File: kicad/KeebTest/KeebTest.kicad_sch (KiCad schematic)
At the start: 19 parts, among them U1 Arduino_Pro_Micro

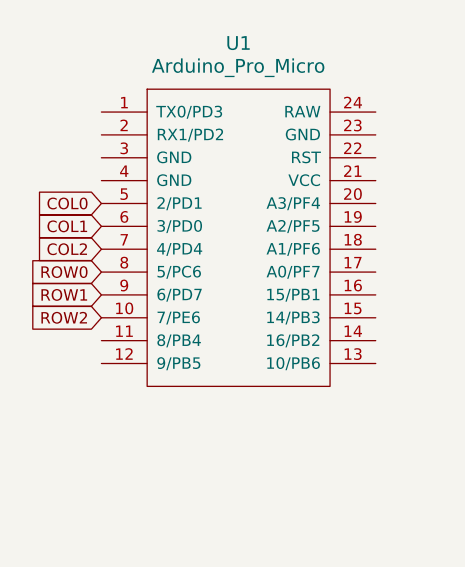
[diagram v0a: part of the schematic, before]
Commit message: update size
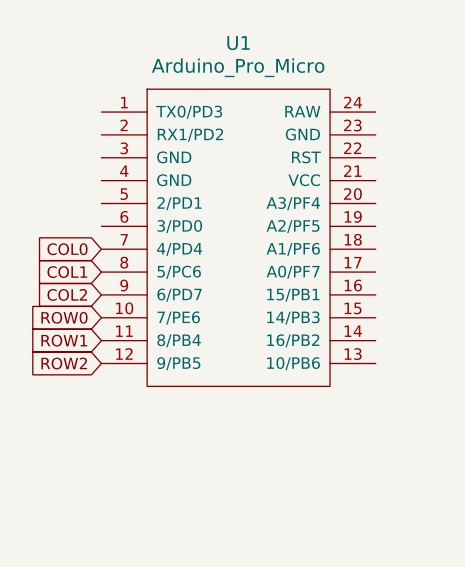
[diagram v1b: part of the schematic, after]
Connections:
- net COL0: now also U1.7 (4/PD4); no longer U1.5 (2/PD1)
- net COL1: now also U1.8 (5/PC6); no longer U1.6 (3/PD0)
- net COL2: now also U1.9 (6/PD7); no longer U1.7 (4/PD4)
- net ROW0: now also U1.10 (7/PE6); no longer U1.8 (5/PC6)
- net ROW1: now also U1.11 (8/PB4); no longer U1.9 (6/PD7)
- net ROW2: now also U1.12 (9/PB5); no longer U1.10 (7/PE6)
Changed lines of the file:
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@@
     (stroke (width 0) (type default))
   )
-  (global_label "COL0" (shape input) (at 30.48 57.15 180) (fields_autoplaced)
+  (global_label "ROW0" (shape input) (at 30.48 69.85 180) (fields_autoplaced)
     (effects (font (size 1.27 1.27)) (justify right))
-    (property "Intersheetrefs" "${INTERSHEET_REFS}" (at 22.6567 57.15 0)
+    (property "Intersheetrefs" "${INTERSHEET_REFS}" (at 22.2334 69.85 0)
       (effects (font (size 1.27 1.27)) (justify right) hide)
     )
   )
-  (global_label "COL1" (shape input) (at 30.48 59.69 180) (fields_autoplaced)
+  (global_label "ROW1" (shape input) (at 30.48 72.39 180) (fields_autoplaced)
     (effects (font (size 1.27 1.27)) (justify right))
-    (property "Intersheetrefs" "${INTERSHEET_REFS}" (at 22.6567 59.69 0)
+    (property "Intersheetrefs" "${INTERSHEET_REFS}" (at 22.2334 72.39 0)
       (effects (font (size 1.27 1.27)) (justify right) hide)
     )
   )
-  (global_label "ROW1" (shape input) (at 30.48 67.31 180) (fields_autoplaced)
+  (global_label "COL1" (shape input) (at 30.48 64.77 180) (fields_autoplaced)
     (effects (font (size 1.27 1.27)) (justify right))
-    (property "Intersheetrefs" "${INTERSHEET_REFS}" (at 22.2334 67.31 0)
+    (property "Intersheetrefs" "${INTERSHEET_REFS}" (at 22.6567 64.77 0)
+      (effects (font (size 1.27 1.27)) (justify right) hide)
+    )
+  )
+  (global_label "COL0" (shape input) (at 30.48 62.23 180) (fields_autoplaced)
+    (effects (font (size 1.27 1.27)) (justify right))
+    (property "Intersheetrefs" "${INTERSHEET_REFS}" (at 22.6567 62.23 0)
+      (effects (font (size 1.27 1.27)) (justify right) hide)
+    )
+  )
+  (global_label "ROW2" (shape input) (at 30.48 74.93 180) (fields_autoplaced)
+    (effects (font (size 1.27 1.27)) (justify right))
+    (property "Intersheetrefs" "${INTERSHEET_REFS}" (at 22.2334 74.93 0)
       (effects (font (size 1.27 1.27)) (justify right) hide)
     )
@@
     )
   )
-  (global_label "ROW2" (shape input) (at 30.48 69.85 180) (fields_autoplaced)
-    (effects (font (size 1.27 1.27)) (justify right))
-    (property "Intersheetrefs" "${INTERSHEET_REFS}" (at 22.2334 69.85 0)
-      (effects (font (size 1.27 1.27)) (justify right) hide)
-    )
-  )
   (global_label "ROW1" (shape input) (at 133.35 85.09 0) (fields_autoplaced)
     (effects (font (size 1.27 1.27)) (justify left))
     (property "Intersheetrefs" "${INTERSHEET_REFS}" (at 141.5966 85.09 0)
       (effects (font (size 1.27 1.27)) (justify left) hide)
-    )
-  )
-  (global_label "ROW0" (shape input) (at 30.48 64.77 180) (fields_autoplaced)
-    (effects (font (size 1.27 1.27)) (justify right))
-    (property "Intersheetrefs" "${INTERSHEET_REFS}" (at 22.2334 64.77 0)
-      (effects (font (size 1.27 1.27)) (justify right) hide)
     )
   )
@@
     )
   )
-  (global_label "COL2" (shape input) (at 30.48 62.23 180) (fields_autoplaced)
-    (effects (font (size 1.27 1.27)) (justify right))
-    (property "Intersheetrefs" "${INTERSHEET_REFS}" (at 22.6567 62.23 0)
-      (effects (font (size 1.27 1.27)) (justify right) hide)
-    )
-  )
   (global_label "ROW2" (shape input) (at 133.35 106.68 0) (fields_autoplaced)
     (effects (font (size 1.27 1.27)) (justify left))
@@
     )
   )
+  (global_label "COL2" (shape input) (at 30.48 67.31 180) (fields_autoplaced)
+    (effects (font (size 1.27 1.27)) (justify right))
+    (property "Intersheetrefs" "${INTERSHEET_REFS}" (at 22.6567 67.31 0)
+      (effects (font (size 1.27 1.27)) (justify right) hide)
+    )
+  )

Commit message: update size
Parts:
- added H1, H2, H3, H4: MountingHole, MountingHole:MountingHole_2.1mm, symbol Mechanical:MountingHole
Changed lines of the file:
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@@
+    )
+  )
+  (symbol (lib_id "Mechanical:MountingHole") (at 154.94 106.68 0) (unit 1)
+    (in_bom yes) (on_board yes) (dnp no) (fields_autoplaced)
+    (property "Reference" "H2" (at 157.48 105.41 0)
+      (effects (font (size 1.27 1.27)) (justify left))
+    )
+    (property "Value" "MountingHole" (at 157.48 107.95 0)
+      (effects (font (size 1.27 1.27)) (justify left))
+    )
+    (property "Footprint" "MountingHole:MountingHole_2.1mm" (at 154.94 106.68 0)
+      (effects (font (size 1.27 1.27)) hide)
+    )
+    (property "Datasheet" "~" (at 154.94 106.68 0)
+      (effects (font (size 1.27 1.27)) hide)
+    )
+    (instances
+      (project "KeebTest"
+        (path "/98130f4e-5d52-447d-b126-df1d975aefd0"
+          (reference "H2") (unit 1)
+        )
+      )
+    )
+  )
+  (symbol (lib_id "Mechanical:MountingHole") (at 152.4 30.48 0) (unit 1)
+    (in_bom yes) (on_board yes) (dnp no) (fields_autoplaced)
+    (property "Reference" "H1" (at 154.94 29.21 0)
+      (effects (font (size 1.27 1.27)) (justify left))
+    )
+    (property "Value" "MountingHole" (at 154.94 31.75 0)
+      (effects (font (size 1.27 1.27)) (justify left))
+    )
+    (property "Footprint" "MountingHole:MountingHole_2.1mm" (at 152.4 30.48 0)
+      (effects (font (size 1.27 1.27)) hide)
+    )
+    (property "Datasheet" "~" (at 152.4 30.48 0)
+      (effects (font (size 1.27 1.27)) hide)
+    )
+    (instances
+      (project "KeebTest"
+        (path "/98130f4e-5d52-447d-b126-df1d975aefd0"
+          (reference "H1") (unit 1)
+        )
+      )
     )
   )
@@
     )
   )
+  (symbol (lib_id "Mechanical:MountingHole") (at 27.94 106.68 0) (unit 1)
+    (in_bom yes) (on_board yes) (dnp no) (fields_autoplaced)
+    (property "Reference" "H3" (at 30.48 105.41 0)
+      (effects (font (size 1.27 1.27)) (justify left))
+    )
+    (property "Value" "MountingHole" (at 30.48 107.95 0)
+      (effects (font (size 1.27 1.27)) (justify left))
+    )
+    (property "Footprint" "MountingHole:MountingHole_2.1mm" (at 27.94 106.68 0)
+      (effects (font (size 1.27 1.27)) hide)
+    )
+    (property "Datasheet" "~" (at 27.94 106.68 0)
+      (effects (font (size 1.27 1.27)) hide)
+    )
+    (instances
+      (project "KeebTest"
+        (path "/98130f4e-5d52-447d-b126-df1d975aefd0"
+          (reference "H3") (unit 1)
+        )
+      )
+    )
+  )
   (symbol (lib_id "SCOTTO:Placeholder_Diode") (at 92.71 59.69 90) (unit 1)
     (in_bom yes) (on_board yes) (dnp no) (fields_autoplaced)
@@
         )
       )
+    )
+  )
+  (symbol (lib_id "Mechanical:MountingHole") (at 26.67 30.48 0) (unit 1)
+    (in_bom yes) (on_board yes) (dnp no) (fields_autoplaced)
+    (property "Reference" "H4" (at 29.21 29.21 0)
+      (effects (font (size 1.27 1.27)) (justify left))
+    )
+    (property "Value" "MountingHole" (at 29.21 31.75 0)
+      (effects (font (size 1.27 1.27)) (justify left))
+    )
+    (property "Footprint" "MountingHole:MountingHole_2.1mm" (at 26.67 30.48 0)
+      (effects (font (size 1.27 1.27)) hide)
+    )
+    (property "Datasheet" "~" (at 26.67 30.48 0)
+      (effects (font (size 1.27 1.27)) hide)
+    )
+    (instances
+      (project "KeebTest"
+        (path "/98130f4e-5d52-447d-b126-df1d975aefd0"
+          (reference "H4") (unit 1)
+        )
+      )
